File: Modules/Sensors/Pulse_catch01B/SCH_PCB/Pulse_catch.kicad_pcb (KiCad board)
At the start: 2 copper layers, 40.6 x 30.5 mm, 16 parts, among them J1 HEADER_2x03_PARALLEL, J2 INTENSITY, J3 INT_OUT, M1 HOLE, M2 HOLE, M3 HOLE, M4 HOLE, P1 SMA, U1 MCP6002

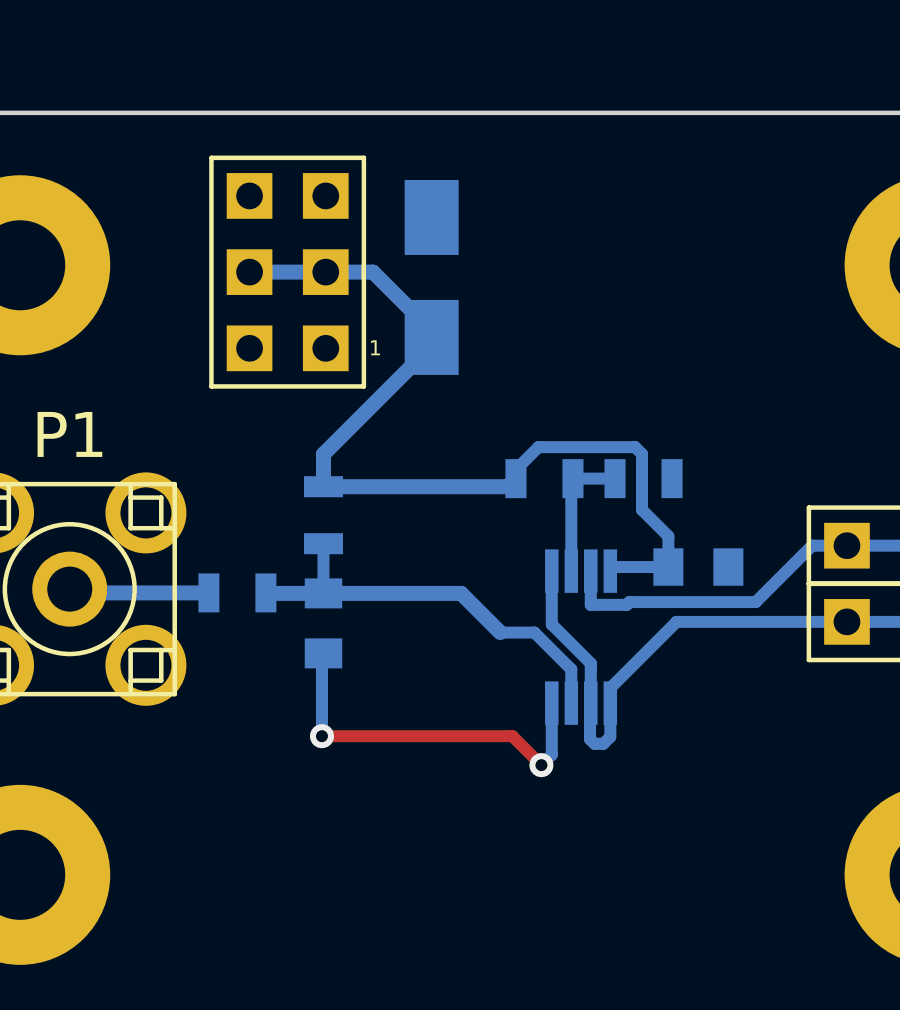
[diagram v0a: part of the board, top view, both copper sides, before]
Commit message: pridani dalsich seriovych odporu pro zvyseni mozne impedance.
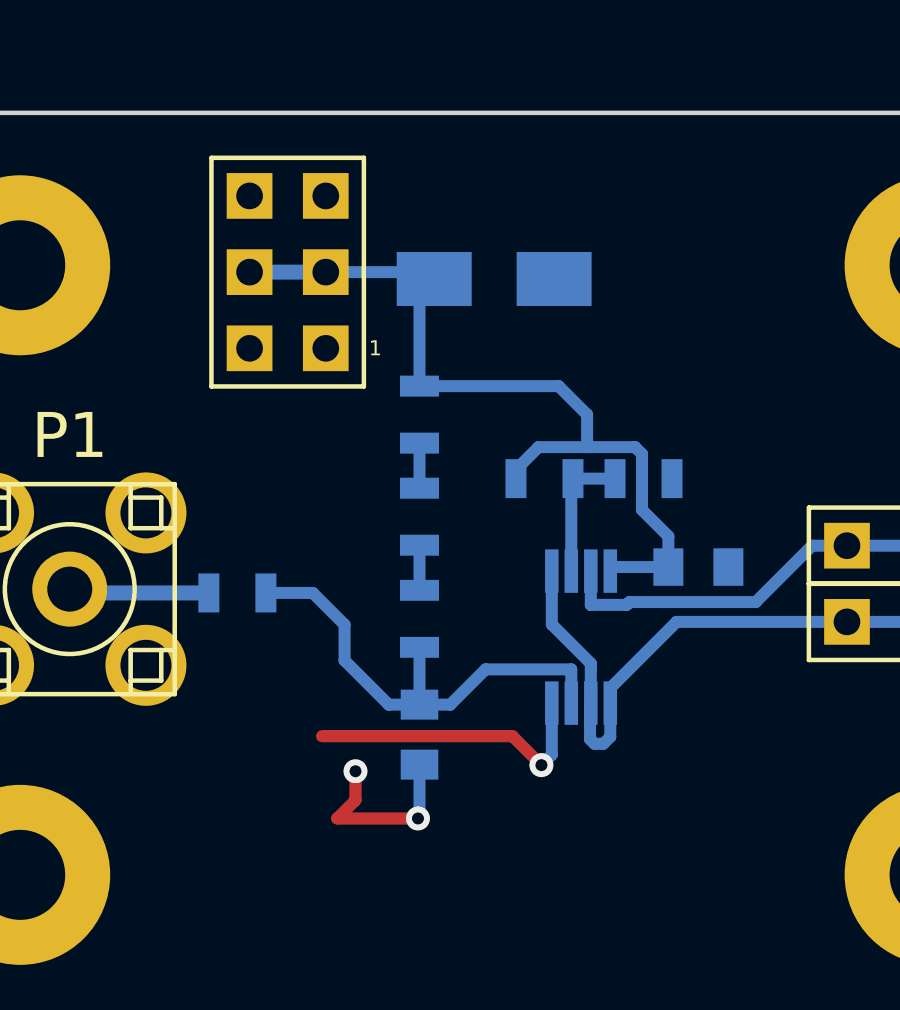
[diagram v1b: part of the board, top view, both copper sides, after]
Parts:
- added R5: 10M, Resistors_SMD:R_0805, B.Cu at (104.7, 76.1)
- added R6: 10M, Resistors_SMD:R_0805, B.Cu at (104.7, 79.5)
- moved C2 4.90 mm to (104.7, 86.8)
- moved R2 4.71 mm to (104.7, 82.9)
- moved D1 2.08 mm to (107.2, 71.6), turned to 180 degrees
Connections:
- R2 pad 1: VDD -> Net-(R2-Pad1)
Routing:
- net GNDA: track 12.7 -> 16.3 mm, vias 2 -> 3
- net VDD: track 31.1 -> 28.1 mm
- net Net-(C2-Pad1): track 14.0 -> 16.1 mm
- net Net-(R5-Pad2): track 0.00 -> 1.50 mm
- net Net-(R2-Pad1): track 0.00 -> 1.50 mm

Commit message: Doplneni popisku na PCB.
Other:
- board text added: "INTENSITY"
- board text added: "INT_OUT"
- board text added: "Kaklik 2016"
- board text added: "POWER"
- board text added: "Pulse_catch01B"
